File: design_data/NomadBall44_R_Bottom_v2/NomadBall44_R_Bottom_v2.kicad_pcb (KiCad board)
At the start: 2 copper layers, 147.4 x 96.5 mm, 14 parts, among them SW21 RotaryEncoder_Switch, SW23 SW_SPDT, U1 XIAO-nRF52840-Plus-SMD

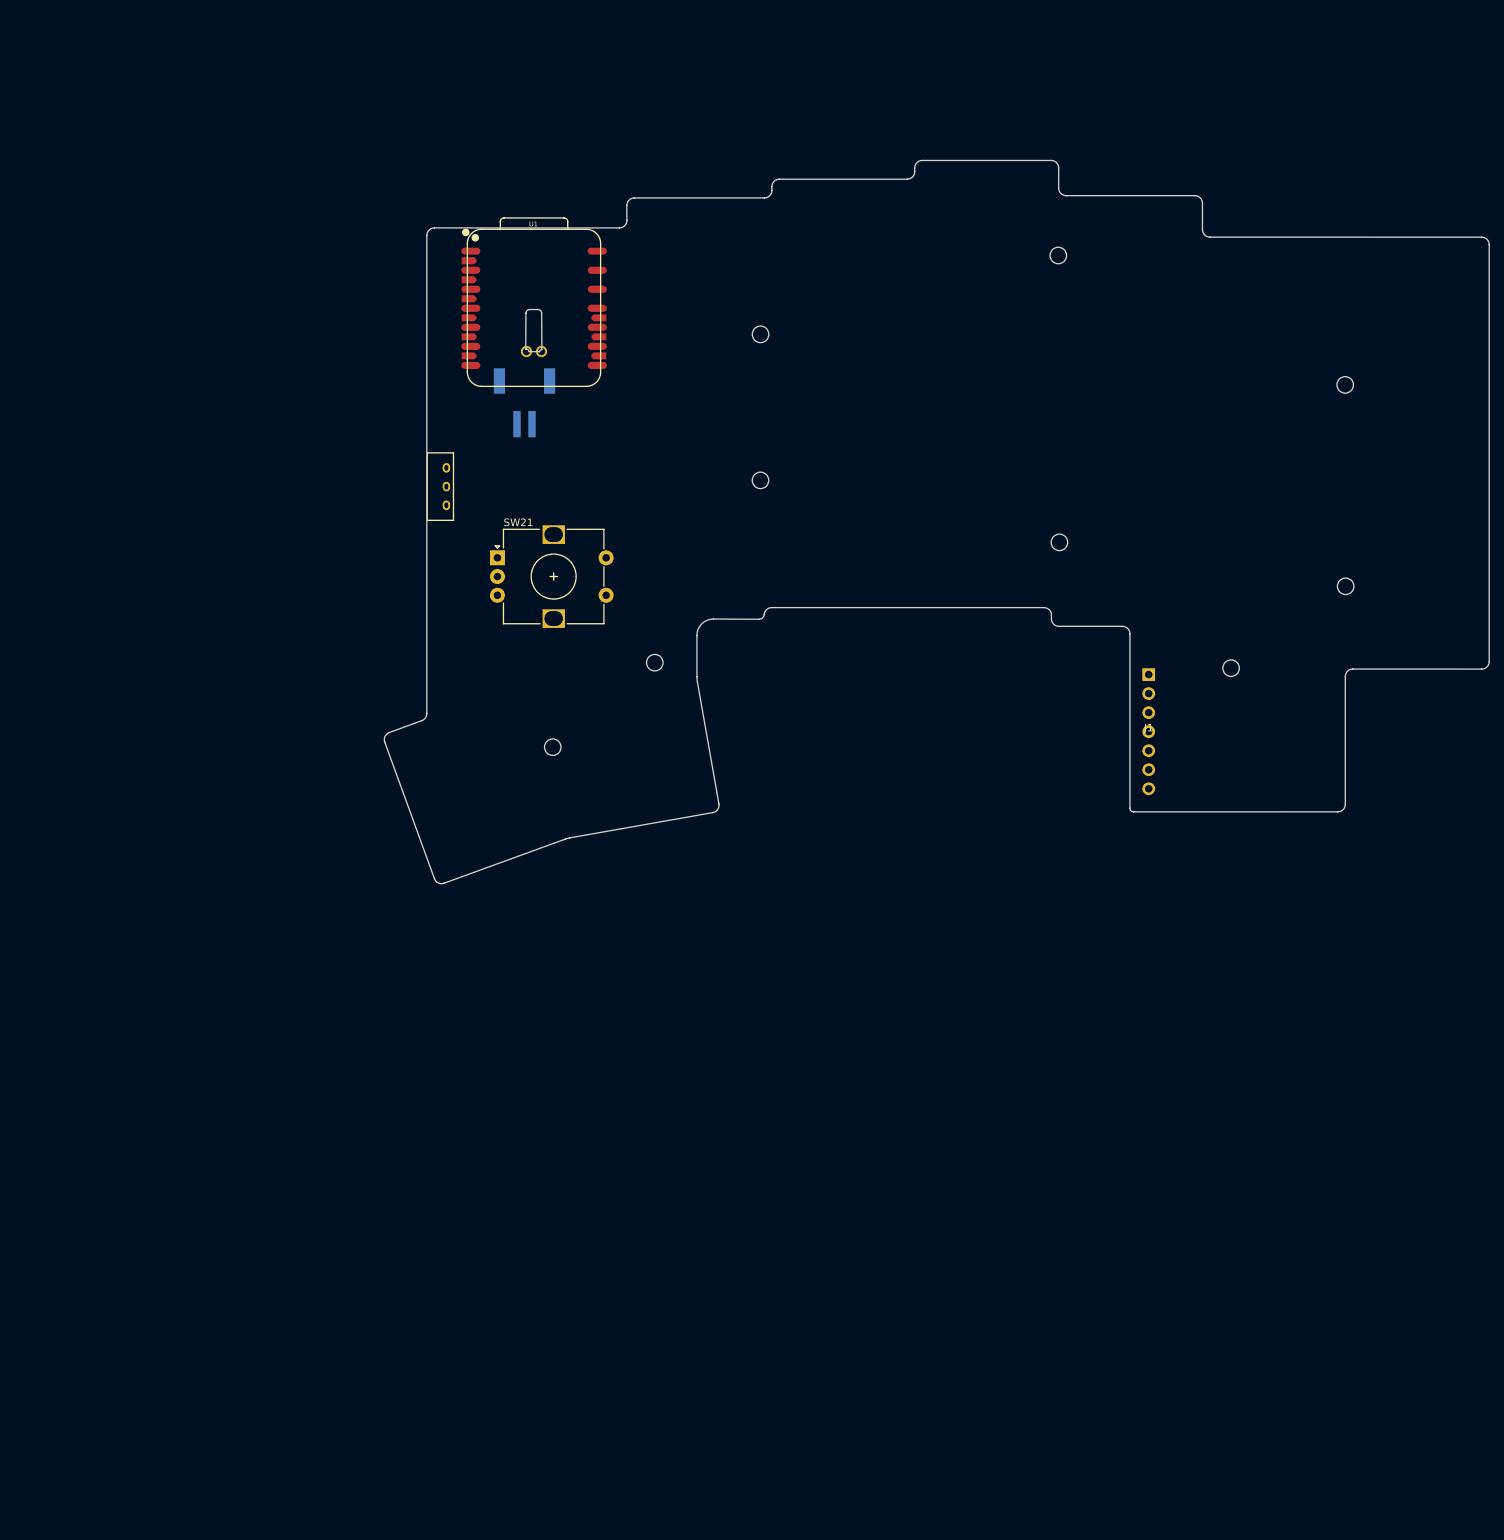
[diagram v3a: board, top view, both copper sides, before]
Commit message: トラックボールケース用のネジ穴を設定
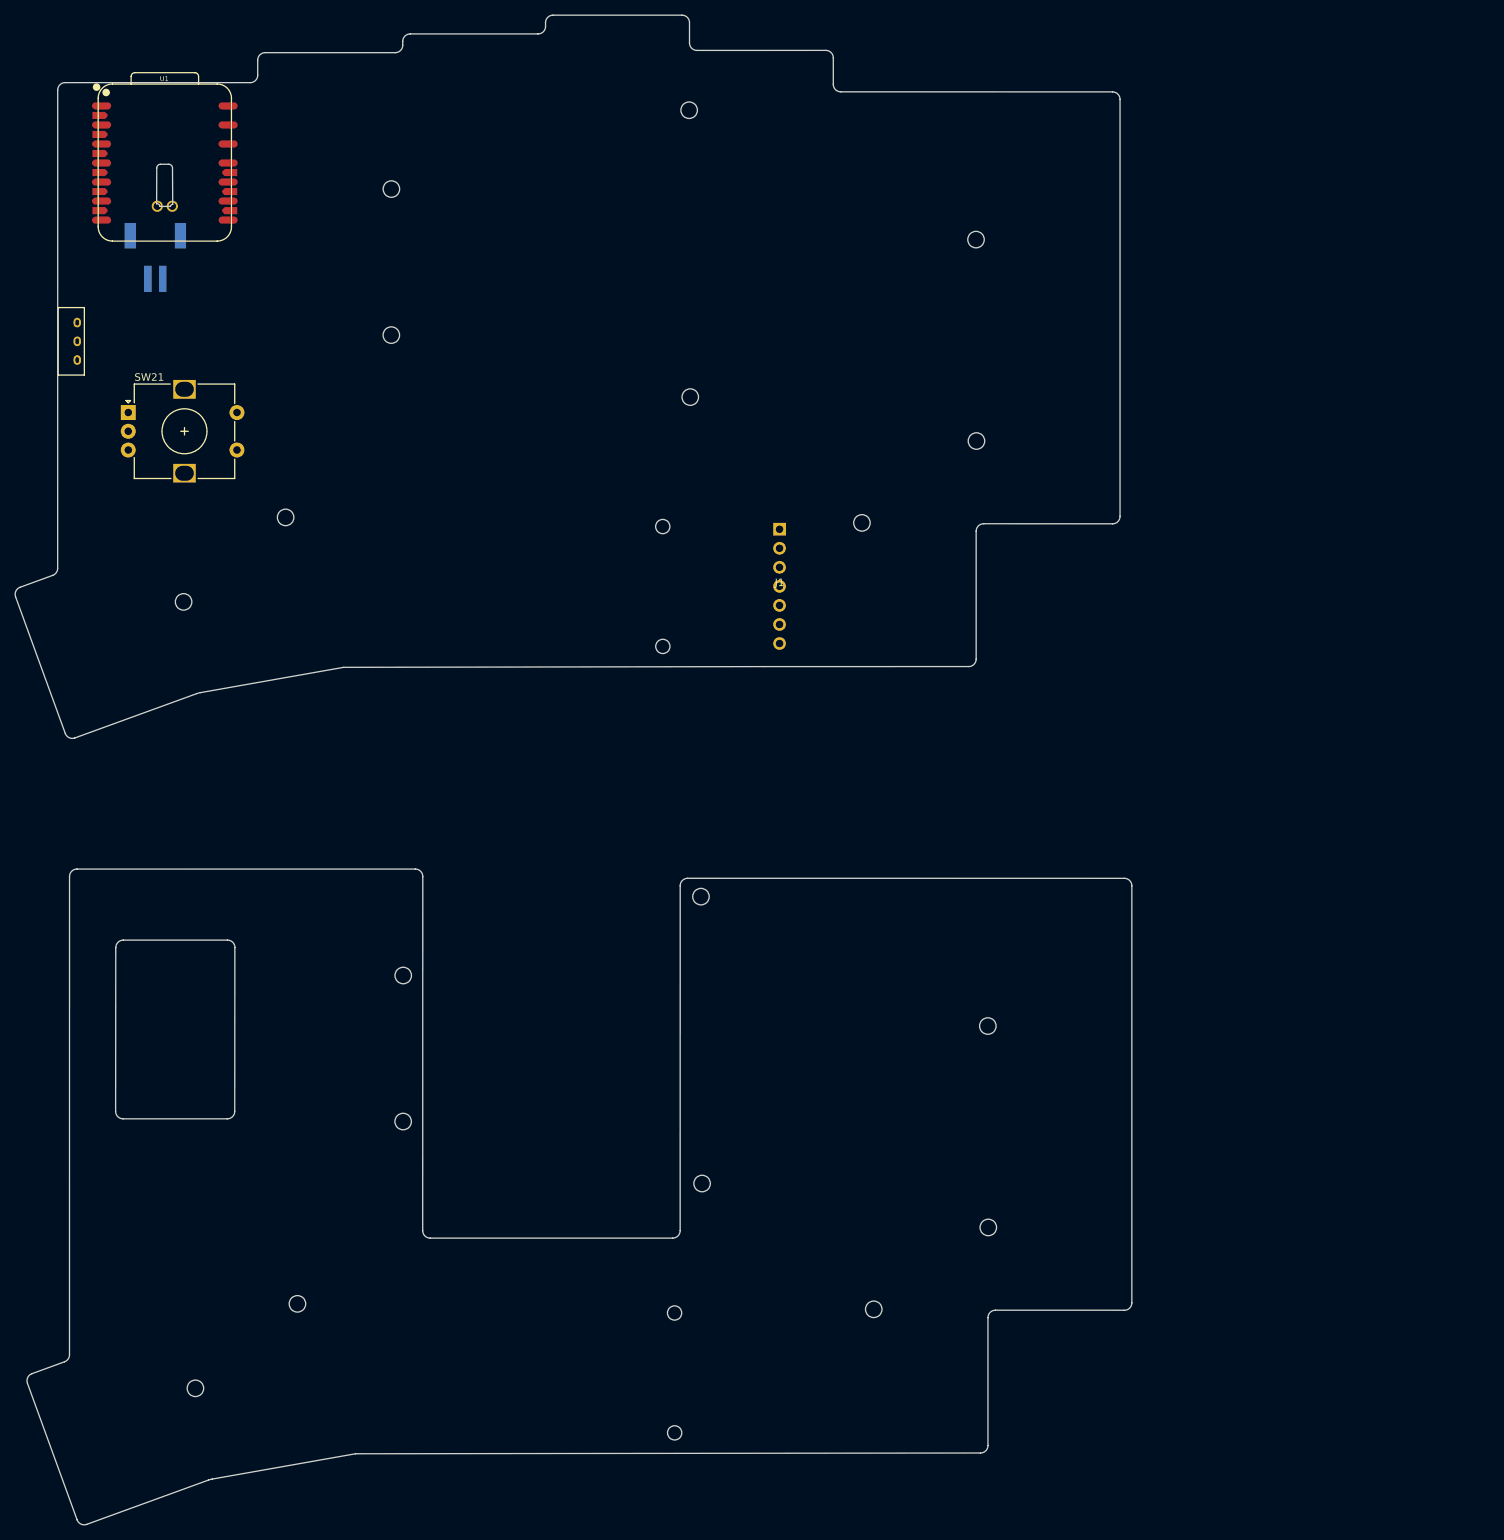
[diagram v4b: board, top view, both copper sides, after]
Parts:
- added REF**: Val**, NomadBall44:m2_Screw_Hole_EdgeCuts, F.Cu at (48.1, 204.5)
- added REF**: Val**, NomadBall44:m1.9_Screw_Hole_EdgeCuts, F.Cu at (112.0, 210.4)
- added REF**: Val**, NomadBall44:m2_Screw_Hole_EdgeCuts, F.Cu at (153.8, 156.2)
- added REF**: Val**, NomadBall44:m2_Screw_Hole_EdgeCuts, F.Cu at (138.6, 194.0)
- added REF**: Val**, NomadBall44:m2_Screw_Hole_EdgeCuts, F.Cu at (153.9, 183.1)
- added REF**: Val**, NomadBall44:m1.9_Screw_Hole_EdgeCuts, F.Cu at (110.5, 105.5)
- added REF**: Val**, NomadBall44:m2_Screw_Hole_EdgeCuts, F.Cu at (75.8, 149.4)
- added REF**: Val**, NomadBall44:m2_Screw_Hole_EdgeCuts, F.Cu at (61.7, 193.2)
- added REF**: Val**, NomadBall44:m2_Screw_Hole_EdgeCuts, F.Cu at (115.5, 138.9)
- added REF**: Val**, NomadBall44:m2_Screw_Hole_EdgeCuts, F.Cu at (75.8, 168.9)
- added REF**: Val**, NomadBall44:m2_Screw_Hole_EdgeCuts, F.Cu at (115.7, 177.2)
- added REF**: Val**, NomadBall44:m1.9_Screw_Hole_EdgeCuts, F.Cu at (110.4, 89.6)
- added REF**: Val**, NomadBall44:m1.9_Screw_Hole_EdgeCuts, F.Cu at (112.0, 194.5)
- moved J1 52.9 mm to (126.0, 97.5)
- moved REF** 52.9 mm to (114.1, 72.3)
- moved REF** 52.9 mm to (114.0, 34.0)
- moved BT1 52.9 mm to (42.8, 56.5)
- moved REF** 52.9 mm to (137.0, 89.1)
- moved REF** 52.9 mm to (152.2, 51.3)
- moved REF** 52.9 mm to (152.3, 78.1)
- moved REF** 52.9 mm to (74.2, 44.5)
- moved REF** 52.9 mm to (74.2, 64.0)
- moved SW21 52.9 mm to (39.1, 74.3)
- moved SW23 52.9 mm to (31.3, 64.8)
- moved REF** 52.9 mm to (60.1, 88.3)
- moved REF** 52.9 mm to (46.5, 99.6)
- moved U1 52.9 mm to (42.6, 41.0)
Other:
- board size 147.4 x 96.5 mm -> 149 x 201.4 mm

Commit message: ボトムプレートに不要なfootprintやedge cutsを削除
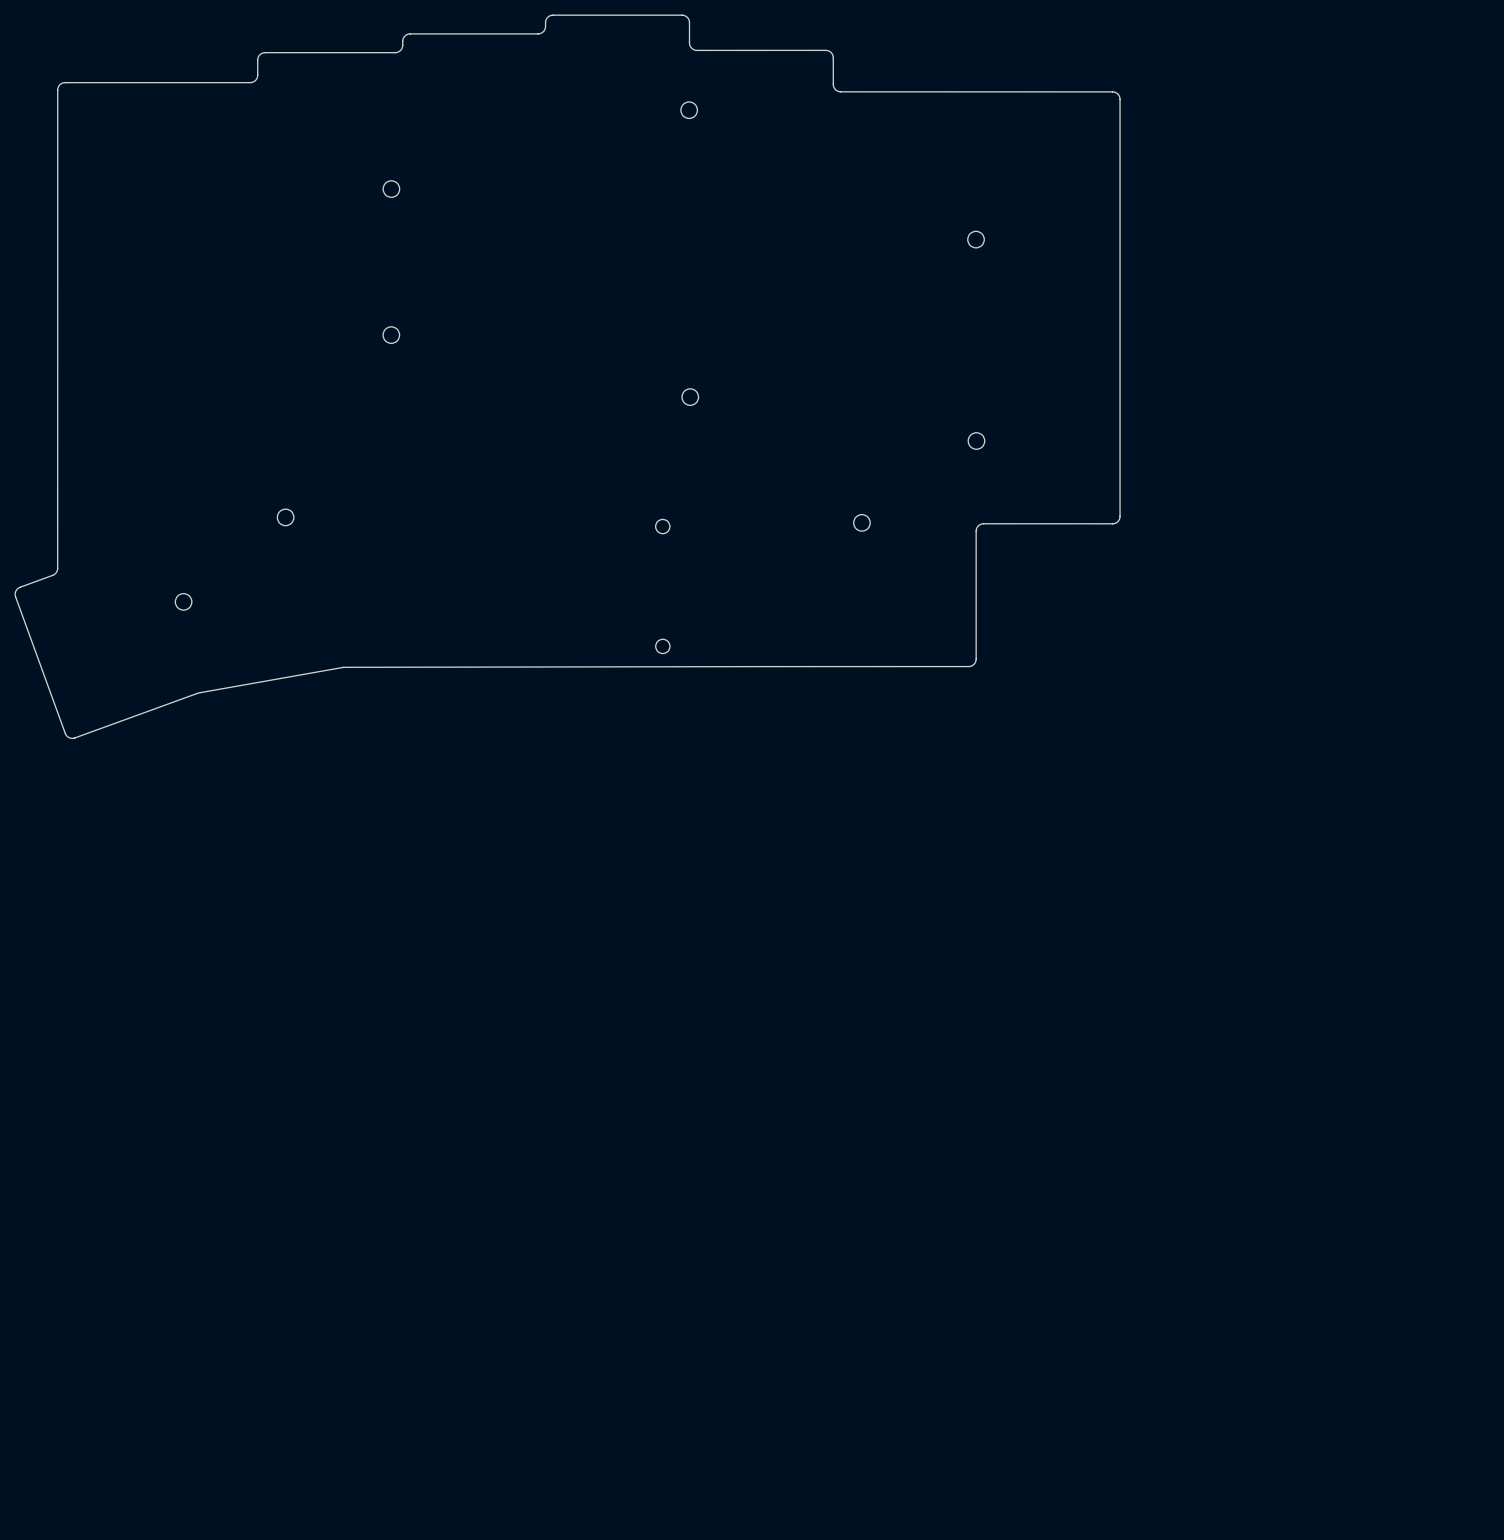
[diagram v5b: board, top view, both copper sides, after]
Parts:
- removed BT1: Battery_Cell, NomadBall44:JST_S2B-PH-SM4-TB
- removed J1: ~, NomadBall44:pmw3610_connector
- removed the REF** at (48.1, 204.5)
- removed the REF** at (112.0, 210.4)
- removed the REF** at (153.8, 156.2)
- removed the REF** at (138.6, 194.0)
- removed the REF** at (153.9, 183.1)
- removed the REF** at (75.8, 149.4)
- removed the REF** at (61.7, 193.2)
- removed the REF** at (115.5, 138.9)
- removed the REF** at (75.8, 168.9)
- removed the REF** at (115.7, 177.2)
- removed the REF** at (112.0, 194.5)
- removed SW21: RotaryEncoder_Switch, Rotary_Encoder:RotaryEncoder_Alps_EC12E-Switch_Vertical_H20mm
- removed SW23: SW_SPDT, NomadBall44:TGSW_MSK-12D19
- removed U1: XIAO-nRF52840-Plus-SMD, NomadBall44:XIAO-nRF52840-Plus-ver3
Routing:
- net Bat: track 1.25 -> 0.00 mm
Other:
- board size 149 x 201.4 mm -> 147.4 x 96.5 mm
